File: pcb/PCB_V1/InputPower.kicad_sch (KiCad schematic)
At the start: 14 parts, among them J901 12 V IN / 25 A design, Q901 P-MOSFET reverse-polarity / M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

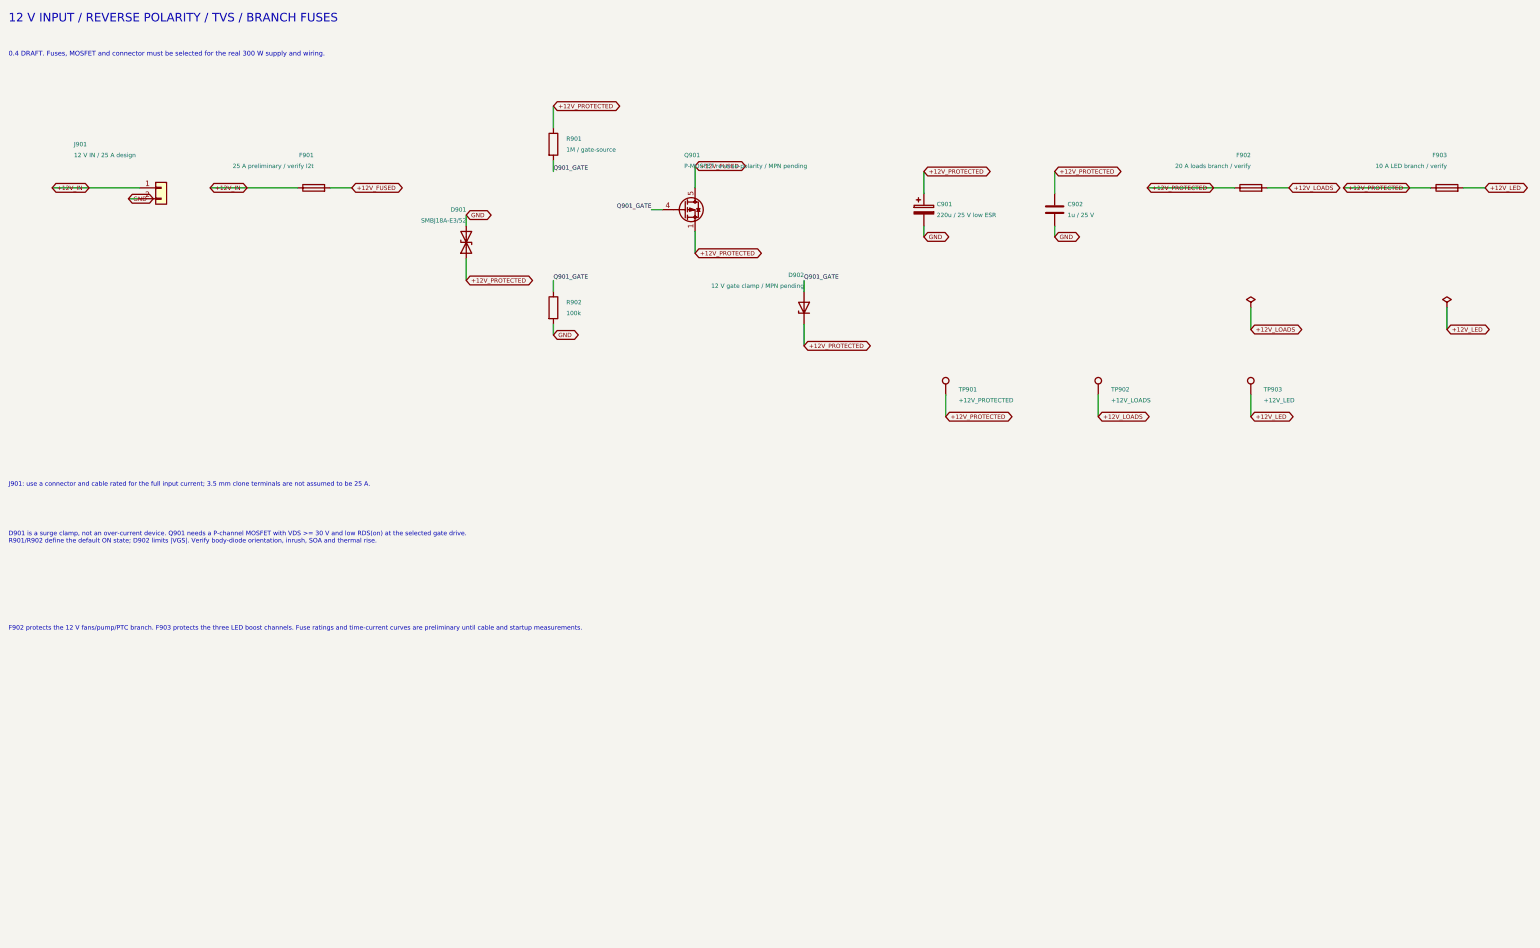
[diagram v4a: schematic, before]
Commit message: pcb: select ideal-diode input protection and regulate heater gate supply
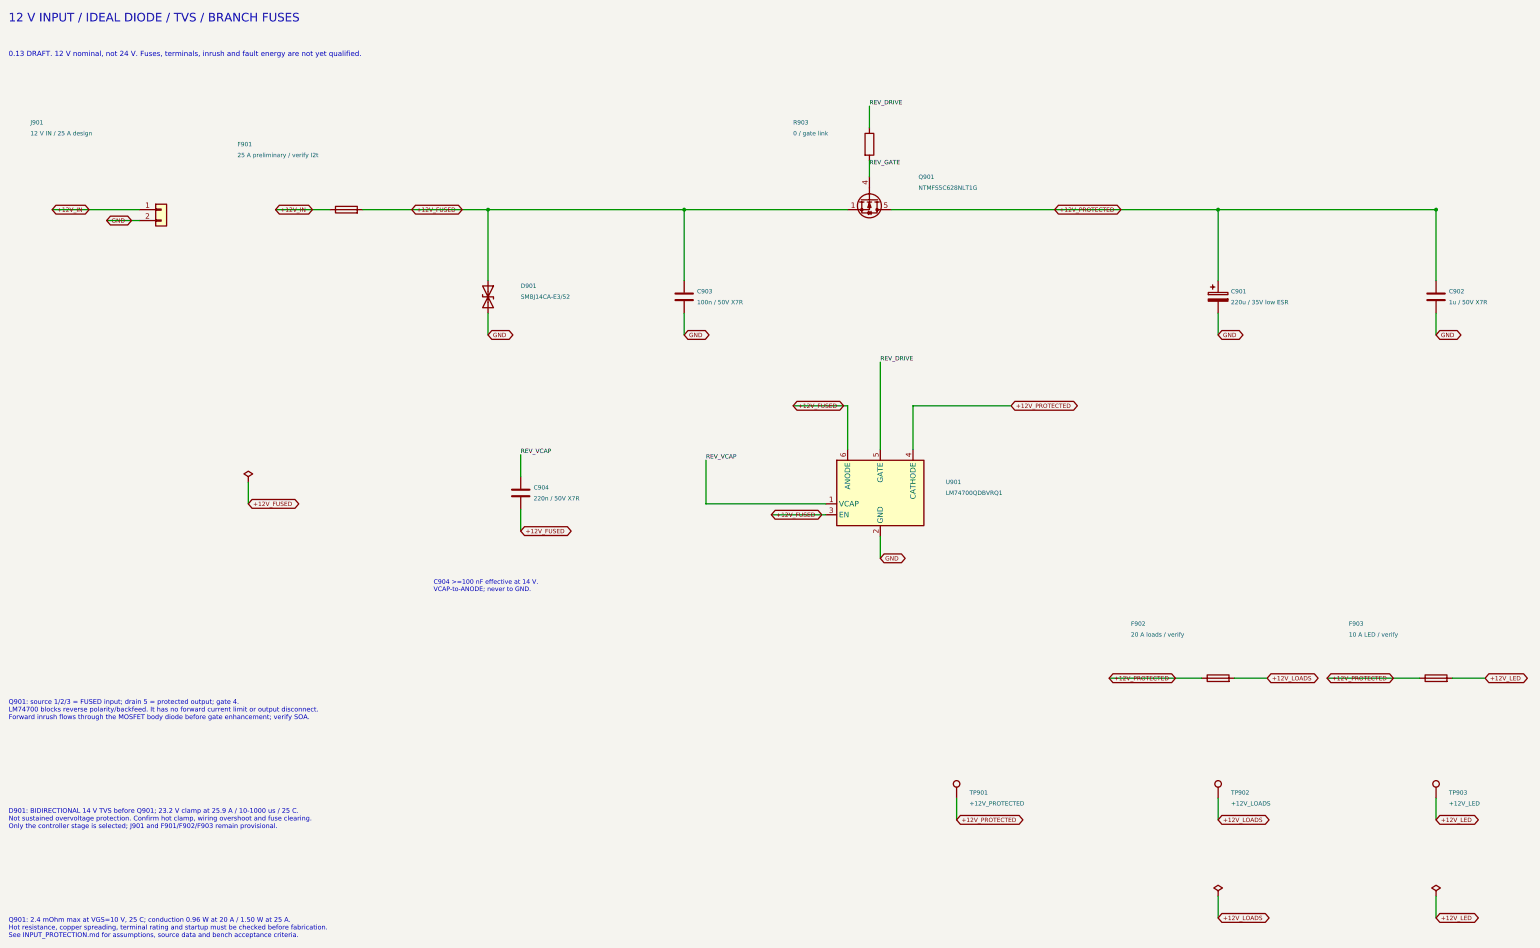
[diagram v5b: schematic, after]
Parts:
- removed D902: 12 V gate clamp / MPN pending, Diode_SMD:D_SOD-323, symbol Device:D_Zener
- removed R901: 1M / gate-source, Resistor_SMD:R_0603_1608Metric, symbol Device:R
- removed R902: 100k, Resistor_SMD:R_0603_1608Metric, symbol Device:R
- added C903: 100n / 50V X7R, Capacitor_SMD:C_0805_2012Metric, symbol Device:C
- added C904: 220n / 50V X7R, Capacitor_SMD:C_0805_2012Metric, symbol Device:C
- added R903: 0 / gate link, Resistor_SMD:R_0603_1608Metric, symbol Device:R
- added U901: LM74700QDBVRQ1, Package_TO_SOT_SMD:SOT-23-6, symbol Power_Management:LM74700
- C901: value 220u / 25 V low ESR -> 220u / 35V low ESR
- C902: value 1u / 25 V -> 1u / 50V X7R
- D901: value SMBJ18A-E3/52 -> SMBJ14CA-E3/52; MPN (none) -> SMBJ14CA-E3/52; Manufacturer (none) -> Vishay
- F902: value 20 A loads branch / verify -> 20 A loads / verify
- F903: value 10 A LED branch / verify -> 10 A LED / verify
- Q901: value P-MOSFET reverse-polarity / MPN pending -> NTMFS5C628NLT1G; footprint Package_SO:PowerPAK_SO-8L_Single -> Package_SO:ONSemi_SO-8FL_488AA; symbol GrowBox:PMOS_PowerPAK_Candidate -> GrowBox:NTMFS5C628NL; LCSC (none) -> C145537; MPN (none) -> NTMFS5C628NLT1G; Manufacturer (none) -> onsemi
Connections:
- net +12V_FUSED: now also D901.1 (A1), Q901.1 (S), Q901.2 (S), Q901.3 (S), C903.1, C904.2, U901.3 (EN), U901.6 (ANODE); no longer Q901.5 (D)
- net +12V_PROTECTED: now also Q901.5 (D), U901.4 (CATHODE); no longer D901.1 (A1), Q901.1 (S), Q901.2 (S), Q901.3 (S)
- net GND: now also C903.2, U901.2 (GND)
- net Q901_GATE renamed REV_GATE
- net REV_GATE: now also R903.2
- new net REV_DRIVE: R903.1, U901.5 (GATE)
- new net REV_VCAP: C904.1, U901.1 (VCAP)
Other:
- note added: "0.13 DRAFT. 12 V nominal, not 24 V. Fuses, terminals, inrush and fault energy are not yet qualified."
- note added: "12 V INPUT / IDEAL DIODE / TVS / BRANCH FUSES"
- note added: "C904 >=100 nF effective at 14 V. VCAP-to-ANODE; never to GND."
- note added: "D901: BIDIRECTIONAL 14 V TVS before Q901; 23.2 V clamp at 25.9 A / 10-1000 us / 25 C. Not sustained overvoltage protection. Confirm hot clamp, wiring overshoot and fuse clearing. Only the controller stage is selected; J901 and F901/F902/F903 remain provisional."
- note added: "Q901: 2.4 mOhm max at VGS=10 V, 25 C; conduction 0.96 W at 20 A / 1.50 W at 25 A. Hot resistance, copper spreading, terminal rating and startup must be checked before fabrication. See INPUT_PROTECTION.md for assumptions, source data and bench acceptance criteria."
- note added: "Q901: source 1/2/3 = FUSED input; drain 5 = protected output; gate 4. LM74700 blocks reverse polarity/backfeed. It has no forward current limit or output disconnect. Forward inrush flows through the MOSFET body diode before gate enhancement; verify SOA."
- note removed: "0.4 DRAFT. Fuses, MOSFET and connector must be selected for the real 300 W supply and wiring."
- note removed: "12 V INPUT / REVERSE POLARITY / TVS / BRANCH FUSES"
- note removed: "D901 is a surge clamp, not an over-current device. Q901 needs a P-channel MOSFET with VDS >= 30 V and low RDS(on) at the selected gate drive. R901/R902 define the default ON state; D902 limits |VGS|. Verify body-diode orientation, inrush, SOA and thermal rise."
- note removed: "F902 protects the 12 V fans/pump/PTC branch. F903 protects the three LED boost channels. Fuse ratings and time-current curves are preliminary until cable and startup measurements."
- note removed: "J901: use a connector and cable rated for the full input current; 3.5 mm clone terminals are not assumed to be 25 A."
- moved on the sheet: C901, C902, D901, F901, F902, F903, J901, Q901, TP901, TP902, TP903

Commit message: pcb: add individual branch fuses and qualified terminal geometry
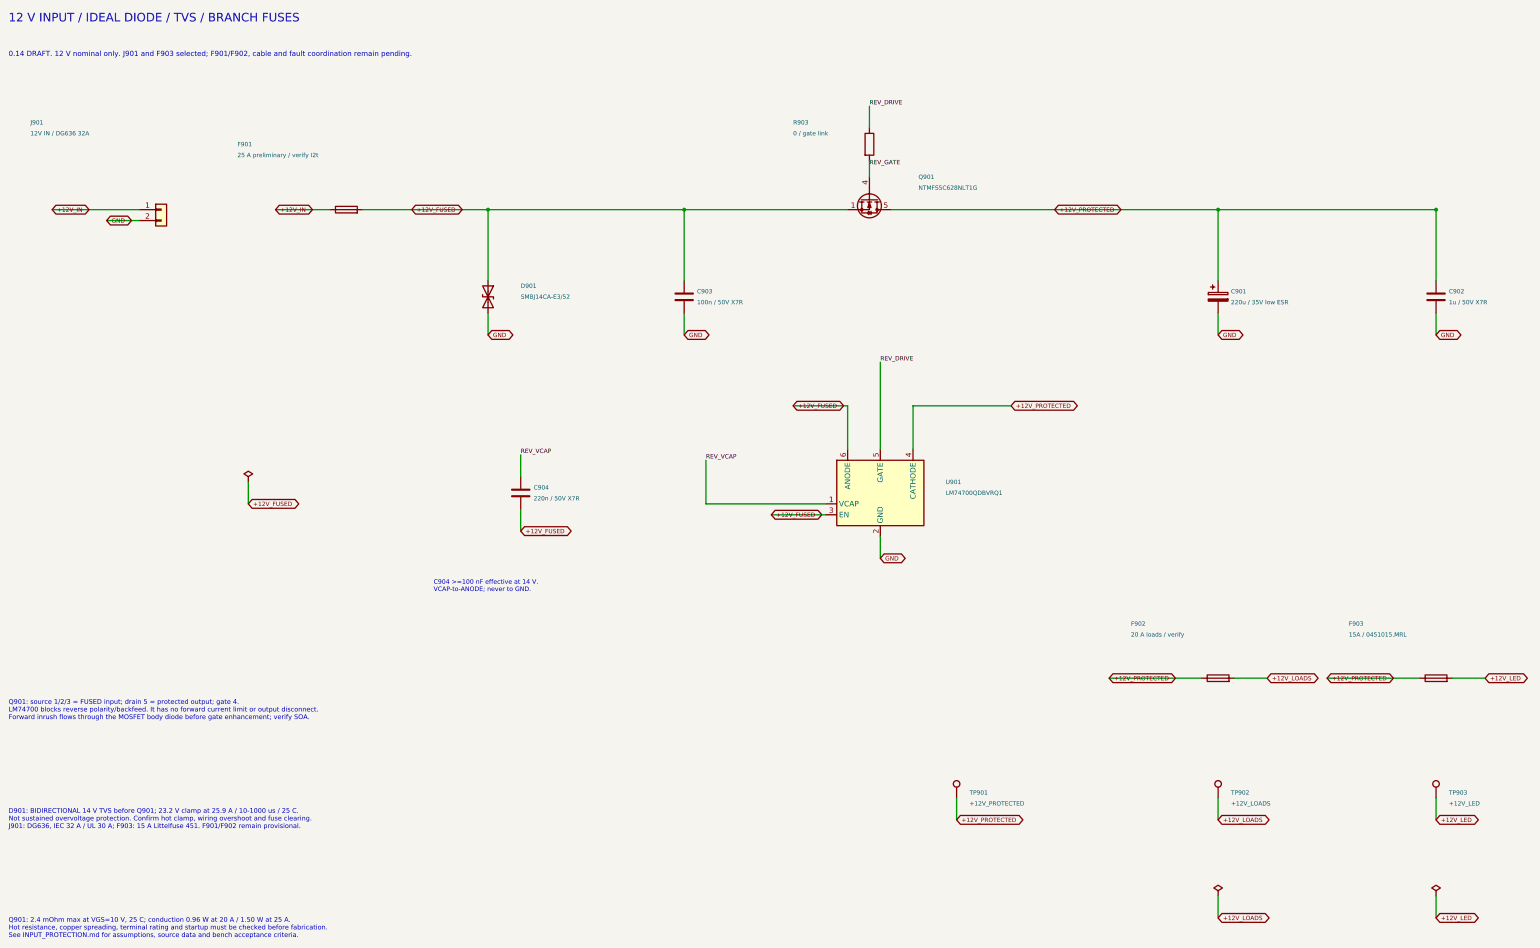
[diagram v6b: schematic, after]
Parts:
- F903: value 10 A LED / verify -> 15A / 0451015.MRL; footprint Fuse:Fuse_2920_7451Metric -> GrowBox:Fuse_Littelfuse_451; LCSC (none) -> C44480; MPN (none) -> 0451015.MRL; Manufacturer (none) -> Littelfuse
- J901: value 12 V IN / 25 A design -> 12V IN / DG636 32A; footprint TerminalBlock_Phoenix:TerminalBlock_Phoenix_MKDS-1,5-2-5.08_1x02_P5.08mm_Horizontal -> GrowBox:TerminalBlock_DEGSON_DG636_1x02_P7.62mm; LCSC (none) -> C581337; MPN (none) -> DG636-7.62-02P-14-00A(H); Manufacturer (none) -> DEGSON
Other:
- note added: "0.14 DRAFT. 12 V nominal only. J901 and F903 selected; F901/F902, cable and fault coordination remain pending."
- note added: "D901: BIDIRECTIONAL 14 V TVS before Q901; 23.2 V clamp at 25.9 A / 10-1000 us / 25 C. Not sustained overvoltage protection. Confirm hot clamp, wiring overshoot and fuse clearing. J901: DG636, IEC 32 A / UL 30 A; F903: 15 A Littelfuse 451. F901/F902 remain provisional."
- note removed: "0.13 DRAFT. 12 V nominal, not 24 V. Fuses, terminals, inrush and fault energy are not yet qualified."
- note removed: "D901: BIDIRECTIONAL 14 V TVS before Q901; 23.2 V clamp at 25.9 A / 10-1000 us / 25 C. Not sustained overvoltage protection. Confirm hot clamp, wiring overshoot and fuse clearing. Only the controller stage is selected; J901 and F901/F902/F903 remain provisional."
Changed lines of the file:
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@@
 		(title "06 - 12 V input protection and branch fuses")
 		(date "2026-09-27")
-		(rev "0.13-DRAFT")
+		(rev "0.14-DRAFT")
 		(company "GrowBox controller")
 		(comment 1 "Prototype design; protection and thermal qualification pending")
@@
 		)
 	)
-	(text "0.13 DRAFT. 12 V nominal, not 24 V. Fuses, terminals, inrush and fault energy are not yet qualified."
+	(text "0.14 DRAFT. 12 V nominal only. J901 and F903 selected; F901/F902, cable and fault coordination remain pending."
 		(at 20.32 24.13 0)
 		(effects
@@
 			)
 		)
-		(property "Value" "12 V IN / 25 A design"
+		(property "Value" "12V IN / DG636 32A"
 			(at 25.4 43.18 0)
 			(effects
@@
 			)
 		)
-		(property "Footprint" "TerminalBlock_Phoenix:TerminalBlock_Phoenix_MKDS-1,5-2-5.08_1x02_P5.08mm_Horizontal"
+		(property "Footprint" "GrowBox:TerminalBlock_DEGSON_DG636_1x02_P7.62mm"
 			(at 55.88 60.96 0)
 			(effects
@@
 			)
 		)
-		(property "Datasheet" ""
+		(property "Datasheet" "https://datasheet.lcsc.com/datasheet/pdf/ccf46534a5d8f09b26d580ef5634ab2c.pdf?productCode=C581337"
 			(at 55.88 60.96 0)
 			(effects
@@
 					(unit 1)
 				)
+			)
+		)
+		(property "Manufacturer" "DEGSON"
+			(at 55.88 60.96 0)
+			(effects
+				(font
+					(size 1 1)
+				)
+				(hide yes)
+				(justify left)
+			)
+		)
+		(property "MPN" "DG636-7.62-02P-14-00A(H)"
+			(at 55.88 60.96 0)
+			(effects
+				(font
+					(size 1 1)
+				)
+				(hide yes)
+				(justify left)
+			)
+		)
+		(property "LCSC" "C581337"
+			(at 55.88 60.96 0)
+			(effects
+				(font
+					(size 1 1)
+				)
+				(hide yes)
+				(justify left)
 			)
 		)
@@
 			)
 		)
-		(property "Value" "10 A LED / verify"
+		(property "Value" "15A / 0451015.MRL"
 			(at 332.74 160.02 90)
 			(effects
@@
 			)
 		)
-		(property "Footprint" "Fuse:Fuse_2920_7451Metric"
+		(property "Footprint" "GrowBox:Fuse_Littelfuse_451"
 			(at 353.06 170.18 90)
 			(effects
@@
 			)
 		)
-		(property "Datasheet" ""
+		(property "Datasheet" "https://www.littelfuse.com/assetdocs/fuse-451-and-453-datasheet?assetguid=533cd5cc-956c-4243-867f-6ab5a62f6ba1"
 			(at 353.06 170.18 90)
 			(effects
@@
 					(unit 1)
 				)
+			)
+		)
+		(property "Manufacturer" "Littelfuse"
+			(at 353.06 170.18 90)
+			(effects
+				(font
+					(size 1 1)
+				)
+				(hide yes)
+				(justify left)
+			)
+		)
+		(property "MPN" "0451015.MRL"
+			(at 353.06 170.18 90)
+			(effects
+				(font
+					(size 1 1)
+				)
+				(hide yes)
+				(justify left)
+			)
+		)
+		(property "LCSC" "C44480"
+			(at 353.06 170.18 90)
+			(effects
+				(font
+					(size 1 1)
+				)
+				(hide yes)
+				(justify left)
 			)
 		)
@@
 		)
 	)
-	(text "D901: BIDIRECTIONAL 14 V TVS before Q901; 23.2 V clamp at 25.9 A / 10-1000 us / 25 C.\nNot sustained overvoltage protection. Confirm hot clamp, wiring overshoot and fuse clearing.\nOnly the controller stage is selected; J901 and F901/F902/F903 remain provisional."
+	(text "D901: BIDIRECTIONAL 14 V TVS before Q901; 23.2 V clamp at 25.9 A / 10-1000 us / 25 C.\nNot sustained overvoltage protection. Confirm hot clamp, wiring overshoot and fuse clearing.\nJ901: DG636, IEC 32 A / UL 30 A; F903: 15 A Littelfuse 451. F901/F902 remain provisional."
 		(at 20.32 200.66 0)
 		(effects
